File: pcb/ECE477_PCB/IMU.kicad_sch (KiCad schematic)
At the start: 9 parts, among them U5 MPU-9250, U6 MPU-6050, U7 LSM6DS3

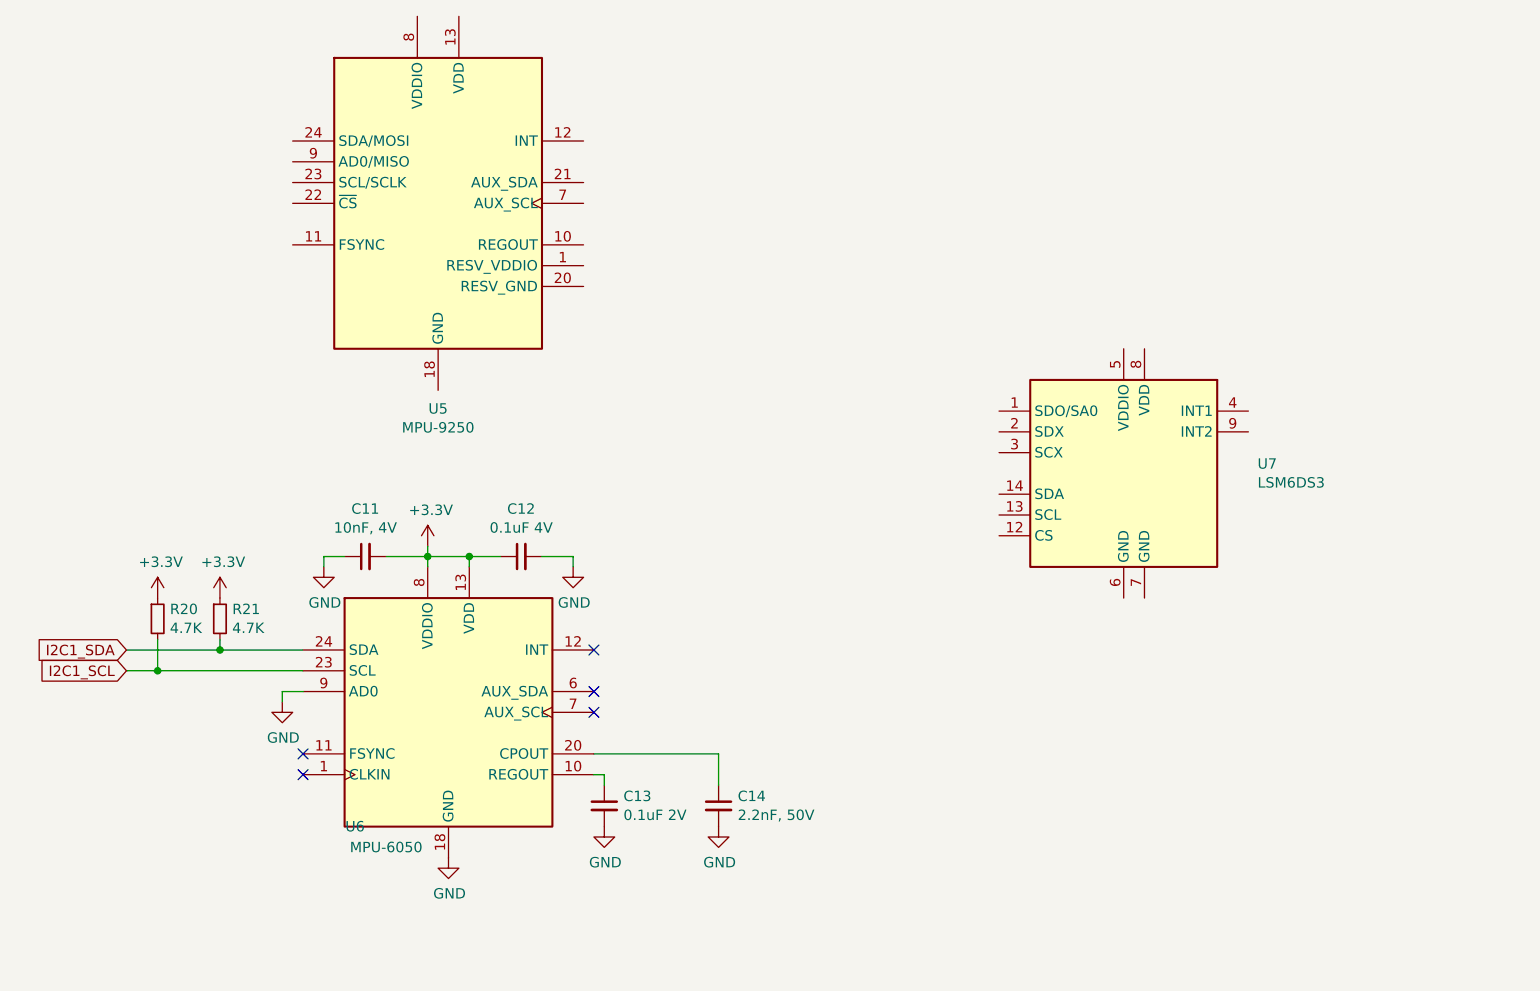
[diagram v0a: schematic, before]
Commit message: modified layout of motor control and power, added minimal initial schematic for LiDAR and footprints
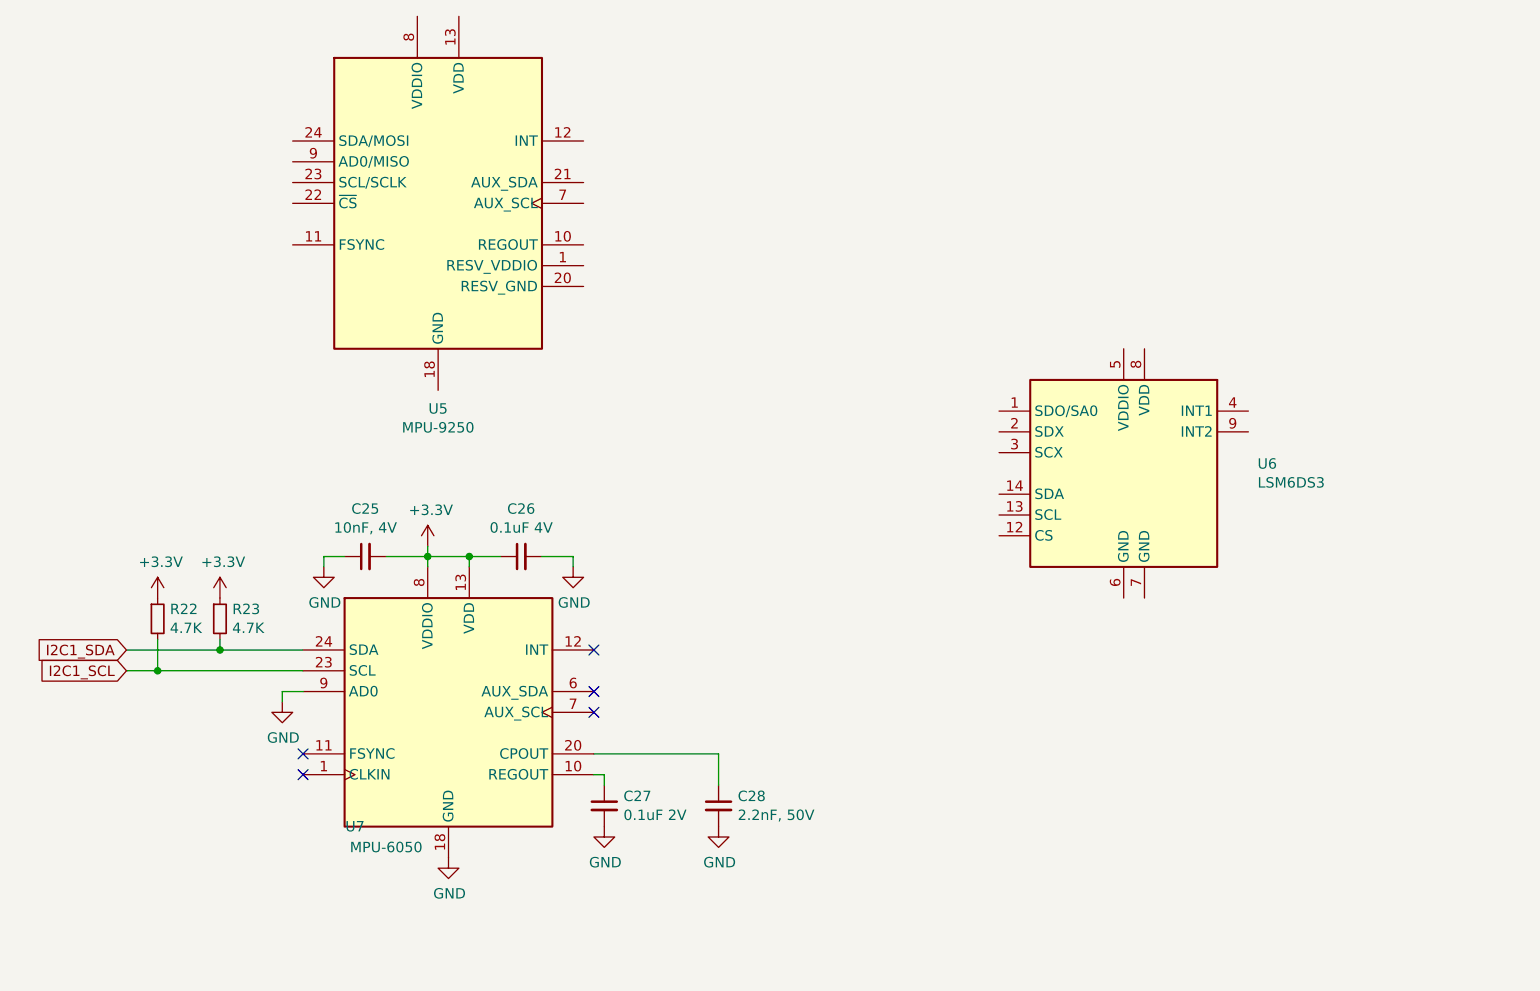
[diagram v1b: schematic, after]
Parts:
- C28: renamed from C14; footprint Capacitor_SMD:C_0805_2012Metric -> Capacitor_SMD:C_0603_1608Metric
- renumbered C11 to C25, C12 to C26, C13 to C27, R20 to R22, R21 to R23, U7 to U6, U6 to U7
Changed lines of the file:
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@@
   (symbol (lib_id "Sensor_Motion:MPU-6050") (at 92.71 97.79 0) (unit 1)
     (in_bom yes) (on_board yes)
-    (property "Reference" "U6" (id 0) (at 81.28 111.76 0))
+    (property "Reference" "U7" (id 0) (at 81.28 111.76 0))
     (property "Value" "MPU-6050" (id 1) (at 85.09 114.3 0))
     (property "Footprint" "Sensor_Motion:InvenSense_QFN-24_4x4mm_P0.5mm" (id 2) (at 92.71 118.11 0)
@@
   (symbol (lib_id "Device:C_Small") (at 125.73 109.22 0) (unit 1)
     (in_bom yes) (on_board yes)
-    (property "Reference" "C14" (id 0) (at 128.0668 108.0516 0)
+    (property "Reference" "C28" (id 0) (at 128.0668 108.0516 0)
       (effects (font (size 1.27 1.27)) (justify left))
     )
@@
       (effects (font (size 1.27 1.27)) (justify left))
     )
-    (property "Footprint" "Capacitor_SMD:C_0805_2012Metric" (id 2) (at 125.73 109.22 0)
+    (property "Footprint" "Capacitor_SMD:C_0603_1608Metric" (id 2) (at 125.73 109.22 0)
       (effects (font (size 1.27 1.27)) hide)
     )
@@
   (symbol (lib_id "Device:C_Small") (at 111.76 109.22 0) (unit 1)
     (in_bom yes) (on_board yes)
-    (property "Reference" "C13" (id 0) (at 114.0968 108.0516 0)
+    (property "Reference" "C27" (id 0) (at 114.0968 108.0516 0)
       (effects (font (size 1.27 1.27)) (justify left))
     )
@@
   (symbol (lib_id "power:GND") (at 111.76 111.76 0) (unit 1)
     (in_bom yes) (on_board yes)
-    (property "Reference" "#PWR0129" (id 0) (at 111.76 118.11 0)
+    (property "Reference" "#PWR063" (id 0) (at 111.76 118.11 0)
       (effects (font (size 1.27 1.27)) hide)
     )
@@
   (symbol (lib_id "power:GND") (at 125.73 111.76 0) (unit 1)
     (in_bom yes) (on_board yes)
-    (property "Reference" "#PWR0130" (id 0) (at 125.73 118.11 0)
+    (property "Reference" "#PWR064" (id 0) (at 125.73 118.11 0)
       (effects (font (size 1.27 1.27)) hide)
     )
@@
   (symbol (lib_id "Device:C_Small") (at 82.55 78.74 90) (unit 1)
     (in_bom yes) (on_board yes)
-    (property "Reference" "C11" (id 0) (at 82.55 72.9234 90))
+    (property "Reference" "C25" (id 0) (at 82.55 72.9234 90))
     (property "Value" "10nF, 4V" (id 1) (at 82.55 75.2348 90))
     (property "Footprint" "Capacitor_SMD:C_0402_1005Metric" (id 2) (at 82.55 78.74 0)
@@
   (symbol (lib_id "power:GND") (at 77.47 80.01 0) (unit 1)
     (in_bom yes) (on_board yes)
-    (property "Reference" "#PWR0126" (id 0) (at 77.47 86.36 0)
+    (property "Reference" "#PWR058" (id 0) (at 77.47 86.36 0)
       (effects (font (size 1.27 1.27)) hide)
     )
@@
   (symbol (lib_id "ECE477_PCB-rescue:+3.3V-power") (at 90.17 77.47 0) (unit 1)
     (in_bom yes) (on_board yes)
-    (property "Reference" "#PWR0128" (id 0) (at 90.17 81.28 0)
+    (property "Reference" "#PWR057" (id 0) (at 90.17 81.28 0)
       (effects (font (size 1.27 1.27)) hide)
     )
@@
   (symbol (lib_id "Device:C_Small") (at 101.6 78.74 90) (unit 1)
     (in_bom yes) (on_board yes)
-    (property "Reference" "C12" (id 0) (at 101.6 72.9234 90))
+    (property "Reference" "C26" (id 0) (at 101.6 72.9234 90))
     (property "Value" "0.1uF 4V" (id 1) (at 101.6 75.2348 90))
     (property "Footprint" "Capacitor_SMD:C_0402_1005Metric" (id 2) (at 101.6 78.74 0)
@@
   (symbol (lib_id "power:GND") (at 107.95 80.01 0) (unit 1)
     (in_bom yes) (on_board yes)
-    (property "Reference" "#PWR0127" (id 0) (at 107.95 86.36 0)
+    (property "Reference" "#PWR059" (id 0) (at 107.95 86.36 0)
       (effects (font (size 1.27 1.27)) hide)
     )
@@
   (symbol (lib_id "Device:R_Small") (at 57.15 86.36 0) (unit 1)
     (in_bom yes) (on_board yes)
-    (property "Reference" "R20" (id 0) (at 58.6486 85.1916 0)
+    (property "Reference" "R22" (id 0) (at 58.6486 85.1916 0)
       (effects (font (size 1.27 1.27)) (justify left))
     )
@@
   (symbol (lib_id "Device:R_Small") (at 64.77 86.36 0) (unit 1)
     (in_bom yes) (on_board yes)
-    (property "Reference" "R21" (id 0) (at 66.2686 85.1916 0)
+    (property "Reference" "R23" (id 0) (at 66.2686 85.1916 0)
       (effects (font (size 1.27 1.27)) (justify left))
     )
@@
   (symbol (lib_id "ECE477_PCB-rescue:+3.3V-power") (at 57.15 83.82 0) (unit 1)
     (in_bom yes) (on_board yes)
-    (property "Reference" "#PWR0123" (id 0) (at 57.15 87.63 0)
+    (property "Reference" "#PWR060" (id 0) (at 57.15 87.63 0)
       (effects (font (size 1.27 1.27)) hide)
     )
@@
   (symbol (lib_id "ECE477_PCB-rescue:+3.3V-power") (at 64.77 83.82 0) (unit 1)
     (in_bom yes) (on_board yes)
-    (property "Reference" "#PWR0124" (id 0) (at 64.77 87.63 0)
+    (property "Reference" "#PWR061" (id 0) (at 64.77 87.63 0)
       (effects (font (size 1.27 1.27)) hide)
     )
@@
   (symbol (lib_id "power:GND") (at 92.71 115.57 0) (unit 1)
     (in_bom yes) (on_board yes)
-    (property "Reference" "#PWR0125" (id 0) (at 92.71 121.92 0)
+    (property "Reference" "#PWR065" (id 0) (at 92.71 121.92 0)
       (effects (font (size 1.27 1.27)) hide)
     )
@@
   (symbol (lib_id "power:GND") (at 72.39 96.52 0) (unit 1)
     (in_bom yes) (on_board yes)
-    (property "Reference" "#PWR0102" (id 0) (at 72.39 102.87 0)
+    (property "Reference" "#PWR062" (id 0) (at 72.39 102.87 0)
       (effects (font (size 1.27 1.27)) hide)
     )
@@
   (symbol (lib_id "Sensor_Motion:LSM6DS3") (at 175.26 68.58 0) (unit 1)
     (in_bom yes) (on_board yes)
-    (property "Reference" "U7" (id 0) (at 191.6176 67.4116 0)
-      (effects (font (size 1.27 1.27)) (justify left))
-    )
+    (property "Reference" "U6" (id 0) (at 191.6176 67.4116 0)
+      (effects (font (size 1.27 1.27)) (justify left))
+    )

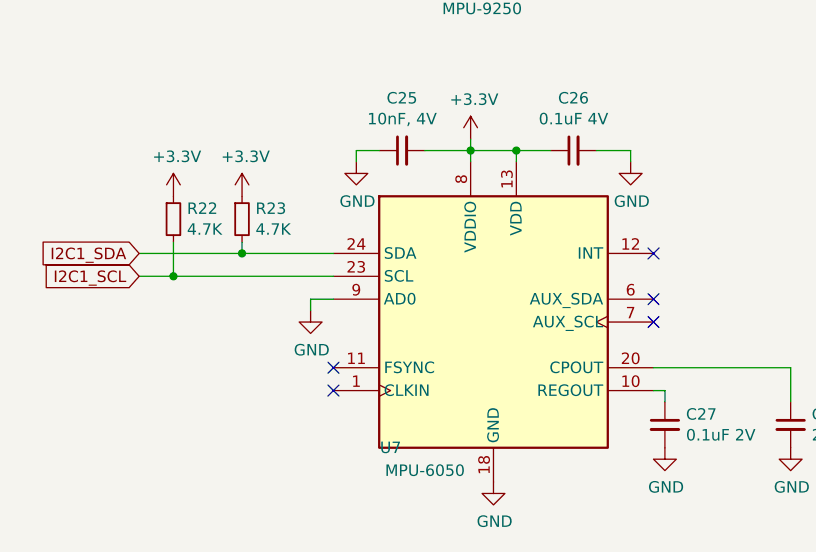
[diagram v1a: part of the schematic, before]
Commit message: updated schematic I2C and UART connections
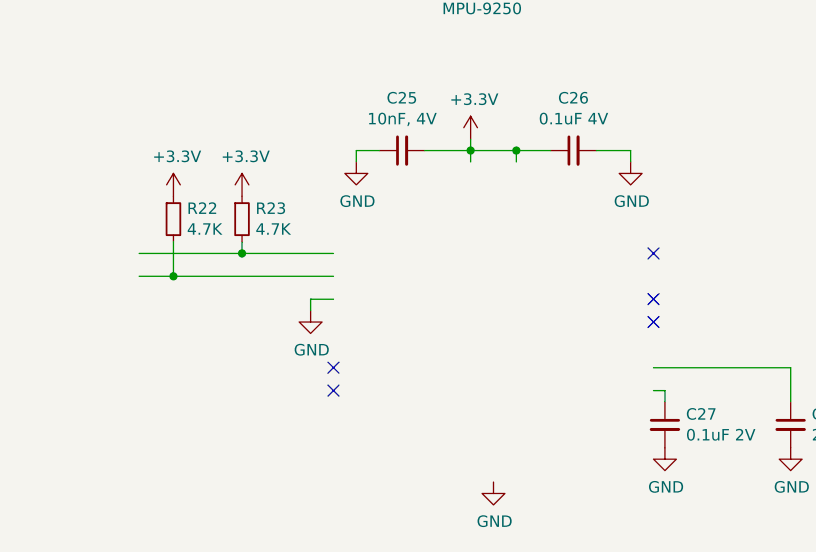
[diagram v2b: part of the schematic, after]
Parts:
- removed U7: MPU-6050, Sensor_Motion:InvenSense_QFN-24_4x4mm_P0.5mm, symbol Sensor_Motion:MPU-6050
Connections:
- net I2C1_SCL: no longer names the net of R22.2
- net I2C1_SDA: no longer names the net of R23.2
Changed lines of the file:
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@@
     (stroke (width 0) (type default) (color 0 0 0 0))
-  )
-  (global_label "I2C1_SDA" (shape input) (at 53.34 90.17 180) (fields_autoplaced)
-    (effects (font (size 1.27 1.27)) (justify right))
-    (property "Intersheet References" "${INTERSHEET_REFS}" (id 0) (at 0 0 0)
-      (effects (font (size 1.27 1.27)) hide)
-    )
-  )
-  (global_label "I2C1_SCL" (shape input) (at 53.34 92.71 180) (fields_autoplaced)
-    (effects (font (size 1.27 1.27)) (justify right))
-    (property "Intersheet References" "${INTERSHEET_REFS}" (id 0) (at 0 0 0)
-      (effects (font (size 1.27 1.27)) hide)
-    )
-  )
-  (symbol (lib_id "Sensor_Motion:MPU-6050") (at 92.71 97.79 0) (unit 1)
-    (in_bom yes) (on_board yes)
-    (property "Reference" "U7" (id 0) (at 81.28 111.76 0))
-    (property "Value" "MPU-6050" (id 1) (at 85.09 114.3 0))
-    (property "Footprint" "Sensor_Motion:InvenSense_QFN-24_4x4mm_P0.5mm" (id 2) (at 92.71 118.11 0)
-      (effects (font (size 1.27 1.27)) hide)
-    )
-    (property "Datasheet" "https://store.invensense.com/datasheets/invensense/MPU-6050_DataSheet_V3%204.pdf" (id 3) (at 92.71 101.6 0)
-      (effects (font (size 1.27 1.27)) hide)
-    )
-    (property "LCSC Part #" "C24112" (id 4) (at 92.71 97.79 0)
-      (effects (font (size 1.27 1.27)) hide)
-    )
-    (property "LCSC" "C24112" (id 5) (at 92.71 97.79 0)
-      (effects (font (size 1.27 1.27)) hide)
-    )
-    (pin "1")
-    (pin "10")
-    (pin "11")
-    (pin "12")
-    (pin "13")
-    (pin "14")
-    (pin "15")
-    (pin "16")
-    (pin "17")
-    (pin "18")
-    (pin "19")
-    (pin "2")
-    (pin "20")
-    (pin "21")
-    (pin "22")
-    (pin "23")
-    (pin "24")
-    (pin "3")
-    (pin "4")
-    (pin "5")
-    (pin "6")
-    (pin "7")
-    (pin "8")
-    (pin "9")
   )
   (symbol (lib_id "Device:C_Small") (at 125.73 109.22 0) (unit 1)
